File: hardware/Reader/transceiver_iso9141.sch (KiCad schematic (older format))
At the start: 8 parts

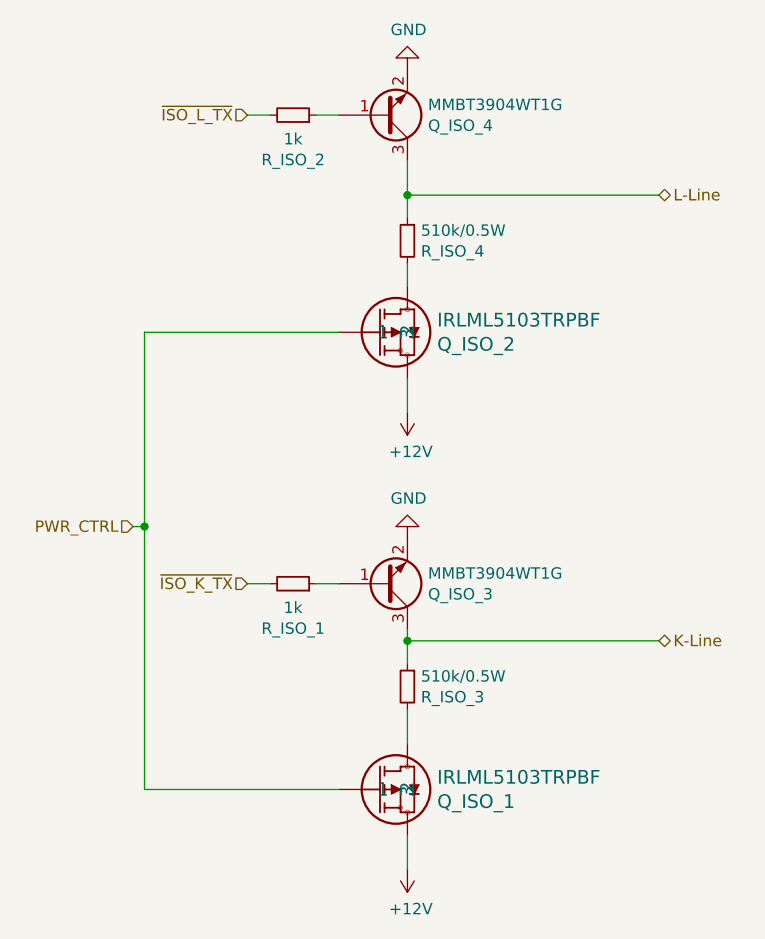
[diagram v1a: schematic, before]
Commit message: Fixed numerous bugs in design for Reader Schematic and PCB
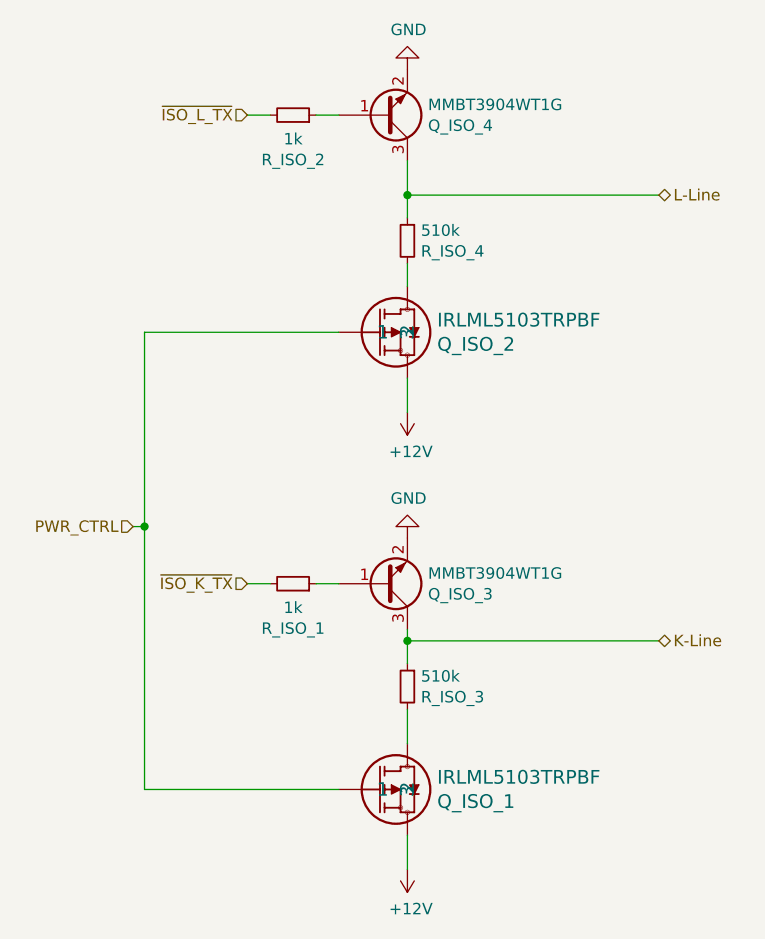
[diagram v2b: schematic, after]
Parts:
- R_ISO_3, R_ISO_4: value 510k/0.5W -> 510k; footprint footprints:RESC2012X70N -> footprints:RESC2012X50N; Manufacturer Panasonic Electronic Components -> Susumu; Part Name ERJ-P06J514V -> RR1220P-514-D; digikeypn P510KADCT-ND -> RR12P510KDCT-ND
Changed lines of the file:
@@
 P 4900 4000
 F 0 "R_ISO_3" H 4841 3954 50  0000 R CNN
-F 1 "510k/0.5W" H 4841 4045 50  0000 R CNN
-F 2 "footprints:RESC2012X70N" H 4900 4000 50  0001 C CNN
-F 3 "https://industrial.panasonic.com/cdbs/www-data/pdf/RDO0000/AOA0000C331.pdf" H 4900 4000 50  0001 C CNN
-F 4 "ERJ-P06J514V" H 4900 4000 50  0001 C CNN "Part Name"
+F 1 "510k" H 4841 4045 50  0000 R CNN
+F 2 "footprints:RESC2012X50N" H 4900 4000 50  0001 C CNN
+F 3 "https://www.susumu.co.jp/common/pdf/n_catalog_partition05_en.pdf" H 4900 4000 50  0001 C CNN
+F 4 "RR1220P-514-D" H 4900 4000 50  0001 C CNN "Part Name"
 F 5 "DigiKey Canada" H 4900 4000 50  0001 C CNN "Vendor"
-F 6 "Panasonic Electronic Components" H 4900 4000 50  0001 C CNN "Manufacturer"
-F 7 "P510KADCT-ND" H 4900 4000 50  0001 C CNN "digikeypn"
+F 6 "Susumu" H 4900 4000 50  0001 C CNN "Manufacturer"
+F 7 "RR12P510KDCT-ND" H 4900 4000 50  0001 C CNN "digikeypn"
 	1    4900 4000
 	-1   0    0    -1
@@
 P 4900 2050
 F 0 "R_ISO_4" H 4841 2004 50  0000 R CNN
-F 1 "510k/0.5W" H 4841 2095 50  0000 R CNN
-F 2 "footprints:RESC2012X70N" H 4900 2050 50  0001 C CNN
-F 3 "https://industrial.panasonic.com/cdbs/www-data/pdf/RDO0000/AOA0000C331.pdf" H 4900 2050 50  0001 C CNN
-F 4 "ERJ-P06J514V" H 4900 2050 50  0001 C CNN "Part Name"
+F 1 "510k" H 4841 2095 50  0000 R CNN
+F 2 "footprints:RESC2012X50N" H 4900 2050 50  0001 C CNN
+F 3 "https://www.susumu.co.jp/common/pdf/n_catalog_partition05_en.pdf" H 4900 2050 50  0001 C CNN
+F 4 "RR1220P-514-D" H 4900 2050 50  0001 C CNN "Part Name"
 F 5 "DigiKey Canada" H 4900 2050 50  0001 C CNN "Vendor"
-F 6 "Panasonic Electronic Components" H 4900 2050 50  0001 C CNN "Manufacturer"
-F 7 "P510KADCT-ND" H 4900 2050 50  0001 C CNN "digikeypn"
+F 6 "Susumu" H 4900 2050 50  0001 C CNN "Manufacturer"
+F 7 "RR12P510KDCT-ND" H 4900 2050 50  0001 C CNN "digikeypn"
 	1    4900 2050
 	-1   0    0    -1
